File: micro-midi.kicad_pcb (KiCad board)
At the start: 2 copper layers, 40 x 27.5 mm, 14 parts, among them J1 AudioJack3, J2 Conn_01x04_Male, J3 AudioJack3, U1 74HC04, U2 6N137

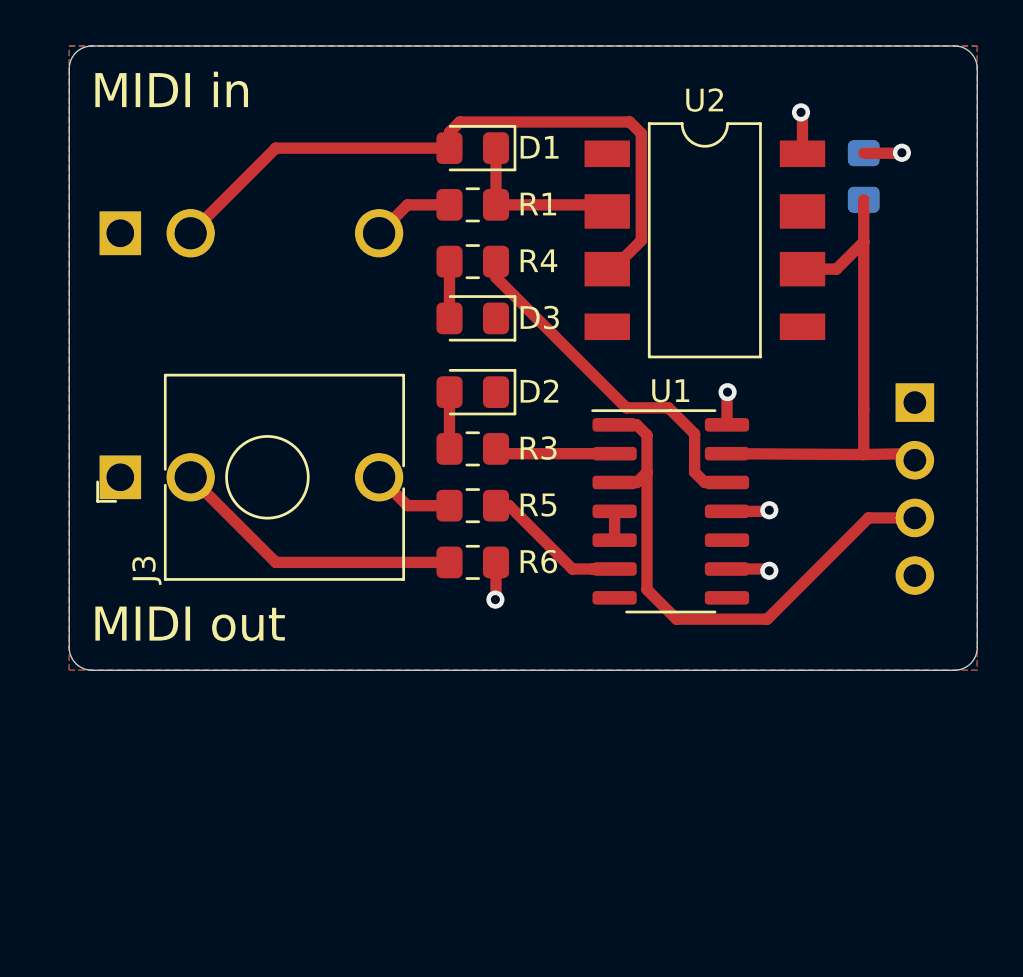
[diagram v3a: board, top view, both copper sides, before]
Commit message: fix accidentally flipped parts
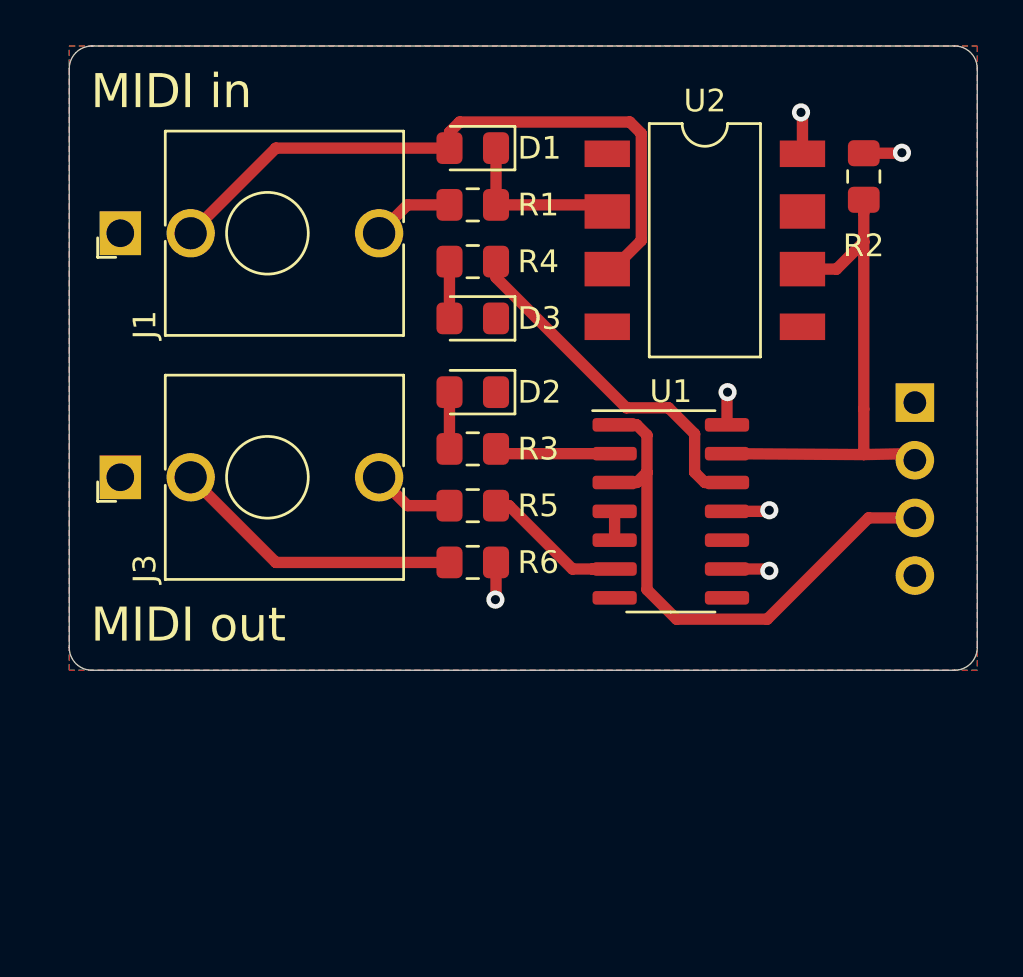
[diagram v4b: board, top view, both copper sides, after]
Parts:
- J1, R2: moved to F.Cu
- turned J1 to 90 degrees
- turned R2 to 90 degrees
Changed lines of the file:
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@@
   )
   (setup
-    (last_trace_width 0.5)
+    (last_trace_width 0.25)
     (user_trace_width 0.5)
     (trace_clearance 0.2)
@@
       (outputformat 1)
       (mirror false)
-      (drillshape 1)
+      (drillshape 0)
       (scaleselection 1)
-      (outputdirectory ""))
+      (outputdirectory "plot"))
   )
   (net 0 "")
@@
     )
   )
-  (module Connector_Audio:Jack_3.5mm_QingPu_WQP-PJ398SM_Vertical_CircularHoles (layer B.Cu)
-    (at 72.25 48.25 270)
+  (module Connector_Audio:Jack_3.5mm_QingPu_WQP-PJ398SM_Vertical_CircularHoles (layer F.Cu)
+    (at 72.25 48.25 90)
     (descr "TRS 3.5mm, vertical, Thonkiconn, PCB mount, (http://www.qingpu-electronics.com/en/products/WQP-PJ398SM-362.html)")
     (tags "WQP-PJ398SM WQP-PJ301M-12 TRS 3.5mm mono vertical jack thonkiconn qingpu")
-    (fp_text reference J1 (at -4.03 -1.08 90) (layer B.SilkS)
-      (effects (font (size 1 1) (thickness 0.15)) (justify mirror))
-    )
-    (fp_text value AudioJack3 (at 0 -5 90) (layer B.Fab)
-      (effects (font (size 1 1) (thickness 0.15)) (justify mirror))
-    )
-    (fp_line (start 0 0) (end 0 -2.03) (layer B.Fab) (width 0.1))
-    (fp_circle (center 0 -6.48) (end 1.8 -6.48) (layer B.Fab) (width 0.1))
-    (fp_line (start 4.5 -2.03) (end -4.5 -2.03) (layer B.Fab) (width 0.1))
-    (fp_line (start 5 1.42) (end -5 1.42) (layer B.CrtYd) (width 0.05))
-    (fp_line (start 5 -12.98) (end -5 -12.98) (layer B.CrtYd) (width 0.05))
-    (fp_line (start 5 -12.98) (end 5 1.42) (layer B.CrtYd) (width 0.05))
-    (fp_line (start 4.5 -12.48) (end -4.5 -12.48) (layer B.Fab) (width 0.1))
-    (fp_line (start 4.5 -12.48) (end 4.5 -2.08) (layer B.Fab) (width 0.1))
-    (fp_line (start -1.06 1) (end -0.2 1) (layer B.SilkS) (width 0.12))
-    (fp_line (start -1.06 1) (end -1.06 0.2) (layer B.SilkS) (width 0.12))
-    (fp_circle (center 0 -6.48) (end 1.8 -6.48) (layer B.SilkS) (width 0.12))
-    (fp_line (start -0.35 -1.98) (end -4.5 -1.98) (layer B.SilkS) (width 0.12))
-    (fp_line (start 4.5 -1.98) (end 0.35 -1.98) (layer B.SilkS) (width 0.12))
-    (fp_line (start -0.5 -12.48) (end -4.5 -12.48) (layer B.SilkS) (width 0.12))
-    (fp_line (start 4.5 -12.48) (end 0.5 -12.48) (layer B.SilkS) (width 0.12))
-    (fp_line (start -1.41 -6.02) (end -0.46 -5.07) (layer Dwgs.User) (width 0.12))
-    (fp_line (start -1.42 -6.875) (end 0.4 -5.06) (layer Dwgs.User) (width 0.12))
-    (fp_line (start -1.07 -7.49) (end 1.01 -5.41) (layer Dwgs.User) (width 0.12))
-    (fp_line (start -0.58 -7.83) (end 1.36 -5.89) (layer Dwgs.User) (width 0.12))
-    (fp_line (start 0.09 -7.96) (end 1.48 -6.57) (layer Dwgs.User) (width 0.12))
-    (fp_circle (center 0 -6.48) (end 1.5 -6.48) (layer Dwgs.User) (width 0.12))
-    (fp_line (start 4.5 -1.98) (end 4.5 -12.48) (layer B.SilkS) (width 0.12))
-    (fp_line (start -4.5 -1.98) (end -4.5 -12.48) (layer B.SilkS) (width 0.12))
-    (fp_text user %R (at 0 -8 90) (layer B.Fab)
-      (effects (font (size 1 1) (thickness 0.15)) (justify mirror))
-    )
-    (fp_line (start -4.5 -12.48) (end -4.5 -2.08) (layer B.Fab) (width 0.1))
-    (fp_line (start -5 -12.98) (end -5 1.42) (layer B.CrtYd) (width 0.05))
-    (fp_text user KEEPOUT (at 0 -6.48 270) (layer Cmts.User)
+    (fp_text reference J1 (at -4.03 1.08 270) (layer F.SilkS)
+      (effects (font (size 1 1) (thickness 0.15)))
+    )
+    (fp_text value AudioJack3 (at 0 5 270) (layer F.Fab)
+      (effects (font (size 1 1) (thickness 0.15)))
+    )
+    (fp_line (start 0 0) (end 0 2.03) (layer F.Fab) (width 0.1))
+    (fp_circle (center 0 6.48) (end 1.8 6.48) (layer F.Fab) (width 0.1))
+    (fp_line (start 4.5 2.03) (end -4.5 2.03) (layer F.Fab) (width 0.1))
+    (fp_line (start 5 -1.42) (end -5 -1.42) (layer F.CrtYd) (width 0.05))
+    (fp_line (start 5 12.98) (end -5 12.98) (layer F.CrtYd) (width 0.05))
+    (fp_line (start 5 12.98) (end 5 -1.42) (layer F.CrtYd) (width 0.05))
+    (fp_line (start 4.5 12.48) (end -4.5 12.48) (layer F.Fab) (width 0.1))
+    (fp_line (start 4.5 12.48) (end 4.5 2.08) (layer F.Fab) (width 0.1))
+    (fp_line (start -1.06 -1) (end -0.2 -1) (layer F.SilkS) (width 0.12))
+    (fp_line (start -1.06 -1) (end -1.06 -0.2) (layer F.SilkS) (width 0.12))
+    (fp_circle (center 0 6.48) (end 1.8 6.48) (layer F.SilkS) (width 0.12))
+    (fp_line (start -0.35 1.98) (end -4.5 1.98) (layer F.SilkS) (width 0.12))
+    (fp_line (start 4.5 1.98) (end 0.35 1.98) (layer F.SilkS) (width 0.12))
+    (fp_line (start -0.5 12.48) (end -4.5 12.48) (layer F.SilkS) (width 0.12))
+    (fp_line (start 4.5 12.48) (end 0.5 12.48) (layer F.SilkS) (width 0.12))
+    (fp_line (start -1.41 6.02) (end -0.46 5.07) (layer Dwgs.User) (width 0.12))
+    (fp_line (start -1.42 6.875) (end 0.4 5.06) (layer Dwgs.User) (width 0.12))
+    (fp_line (start -1.07 7.49) (end 1.01 5.41) (layer Dwgs.User) (width 0.12))
+    (fp_line (start -0.58 7.83) (end 1.36 5.89) (layer Dwgs.User) (width 0.12))
+    (fp_line (start 0.09 7.96) (end 1.48 6.57) (layer Dwgs.User) (width 0.12))
+    (fp_circle (center 0 6.48) (end 1.5 6.48) (layer Dwgs.User) (width 0.12))
+    (fp_line (start 4.5 1.98) (end 4.5 12.48) (layer F.SilkS) (width 0.12))
+    (fp_line (start -4.5 1.98) (end -4.5 12.48) (layer F.SilkS) (width 0.12))
+    (fp_text user %R (at 0 8 270) (layer F.Fab)
+      (effects (font (size 1 1) (thickness 0.15)))
+    )
+    (fp_line (start -4.5 12.48) (end -4.5 2.08) (layer F.Fab) (width 0.1))
+    (fp_line (start -5 12.98) (end -5 -1.42) (layer F.CrtYd) (width 0.05))
+    (fp_text user KEEPOUT (at 0 6.48 90) (layer Cmts.User)
       (effects (font (size 0.4 0.4) (thickness 0.051)))
     )
-    (pad T thru_hole circle (at 0 -11.4 90) (size 2.13 2.13) (drill 1.43) (layers *.Cu *.Mask)
+    (pad T thru_hole circle (at 0 11.4 270) (size 2.13 2.13) (drill 1.43) (layers *.Cu *.Mask)
       (net 6 "Net-(J1-PadT)"))
-    (pad S thru_hole rect (at 0 0 90) (size 1.93 1.83) (drill 1.22) (layers *.Cu *.Mask))
-    (pad R thru_hole circle (at 0 -3.1 90) (size 2.13 2.13) (drill 1.42) (layers *.Cu *.Mask)
+    (pad S thru_hole rect (at 0 0 270) (size 1.93 1.83) (drill 1.22) (layers *.Cu *.Mask))
+    (pad R thru_hole circle (at 0 3.1 270) (size 2.13 2.13) (drill 1.42) (layers *.Cu *.Mask)
       (net 1 "Net-(D1-Pad2)"))
     (model ${KISYS3DMOD}/Connector_Audio.3dshapes/Jack_3.5mm_QingPu_WQP-PJ398SM_Vertical.wrl
@@
     )
   )
-  (module Resistor_SMD:R_0805_2012Metric_Pad1.15x1.40mm_HandSolder (layer B.Cu)
-    (at 105 45.75 270)
+  (module Resistor_SMD:R_0805_2012Metric_Pad1.15x1.40mm_HandSolder (layer F.Cu)
+    (at 105 45.75 90)
     (descr "Resistor SMD 0805 (2012 Metric), square (rectangular) end terminal, IPC_7351 nominal with elongated pad for handsoldering. (Body size source: https://docs.google.com/spreadsheets/d/1BsfQQcO9C6DZCsRaXUlFlo91Tg2WpOkGARC1WS5S8t0/edit?usp=sharing), generated with kicad-footprint-generator")
     (tags "resistor handsolder")
     (attr smd)
-    (fp_text reference R2 (at -3.048 0.009 180) (layer B.SilkS)
-      (effects (font (size 1 1) (thickness 0.15)) (justify mirror))
-    )
-    (fp_text value 10K (at 0 -1.65 270) (layer B.Fab)
-      (effects (font (size 1 1) (thickness 0.15)) (justify mirror))
-    )
-    (fp_line (start -1 -0.6) (end -1 0.6) (layer B.Fab) (width 0.1))
-    (fp_line (start -1 0.6) (end 1 0.6) (layer B.Fab) (width 0.1))
-    (fp_line (start 1 0.6) (end 1 -0.6) (layer B.Fab) (width 0.1))
-    (fp_line (start 1 -0.6) (end -1 -0.6) (layer B.Fab) (width 0.1))
-    (fp_line (start -0.261252 0.71) (end 0.261252 0.71) (layer B.SilkS) (width 0.12))
-    (fp_line (start -0.261252 -0.71) (end 0.261252 -0.71) (layer B.SilkS) (width 0.12))
-    (fp_line (start -1.85 -0.95) (end -1.85 0.95) (layer B.CrtYd) (width 0.05))
-    (fp_line (start -1.85 0.95) (end 1.85 0.95) (layer B.CrtYd) (width 0.05))
-    (fp_line (start 1.85 0.95) (end 1.85 -0.95) (layer B.CrtYd) (width 0.05))
-    (fp_line (start 1.85 -0.95) (end -1.85 -0.95) (layer B.CrtYd) (width 0.05))
-    (fp_text user %R (at 0 0 270) (layer B.Fab)
-      (effects (font (size 0.5 0.5) (thickness 0.08)) (justify mirror))
-    )
-    (pad 1 smd roundrect (at -1.025 0 270) (size 1.15 1.4) (layers B.Cu B.Paste B.Mask) (roundrect_rratio 0.217391)
+    (fp_text reference R2 (at -3.048 -0.009 180) (layer F.SilkS)
+      (effects (font (size 1 1) (thickness 0.15)))
+    )
+    (fp_text value 10K (at 0 1.65 90) (layer F.Fab)
+      (effects (font (size 1 1) (thickness 0.15)))
+    )
+    (fp_line (start -1 0.6) (end -1 -0.6) (layer F.Fab) (width 0.1))
+    (fp_line (start -1 -0.6) (end 1 -0.6) (layer F.Fab) (width 0.1))
+    (fp_line (start 1 -0.6) (end 1 0.6) (layer F.Fab) (width 0.1))
+    (fp_line (start 1 0.6) (end -1 0.6) (layer F.Fab) (width 0.1))
+    (fp_line (start -0.261252 -0.71) (end 0.261252 -0.71) (layer F.SilkS) (width 0.12))
+    (fp_line (start -0.261252 0.71) (end 0.261252 0.71) (layer F.SilkS) (width 0.12))
+    (fp_line (start -1.85 0.95) (end -1.85 -0.95) (layer F.CrtYd) (width 0.05))
+    (fp_line (start -1.85 -0.95) (end 1.85 -0.95) (layer F.CrtYd) (width 0.05))
+    (fp_line (start 1.85 -0.95) (end 1.85 0.95) (layer F.CrtYd) (width 0.05))
+    (fp_line (start 1.85 0.95) (end -1.85 0.95) (layer F.CrtYd) (width 0.05))
+    (fp_text user %R (at 0 0 90) (layer F.Fab)
+      (effects (font (size 0.5 0.5) (thickness 0.08)))
+    )
+    (pad 1 smd roundrect (at -1.025 0 90) (size 1.15 1.4) (layers F.Cu F.Paste F.Mask) (roundrect_rratio 0.217391)
       (net 4 "Net-(J2-Pad2)"))
-    (pad 2 smd roundrect (at 1.025 0 270) (size 1.15 1.4) (layers B.Cu B.Paste B.Mask) (roundrect_rratio 0.217391)
+    (pad 2 smd roundrect (at 1.025 0 90) (size 1.15 1.4) (layers F.Cu F.Paste F.Mask) (roundrect_rratio 0.217391)
       (net 3 +5V))
     (model ${KISYS3DMOD}/Resistor_SMD.3dshapes/R_0805_2012Metric.wrl

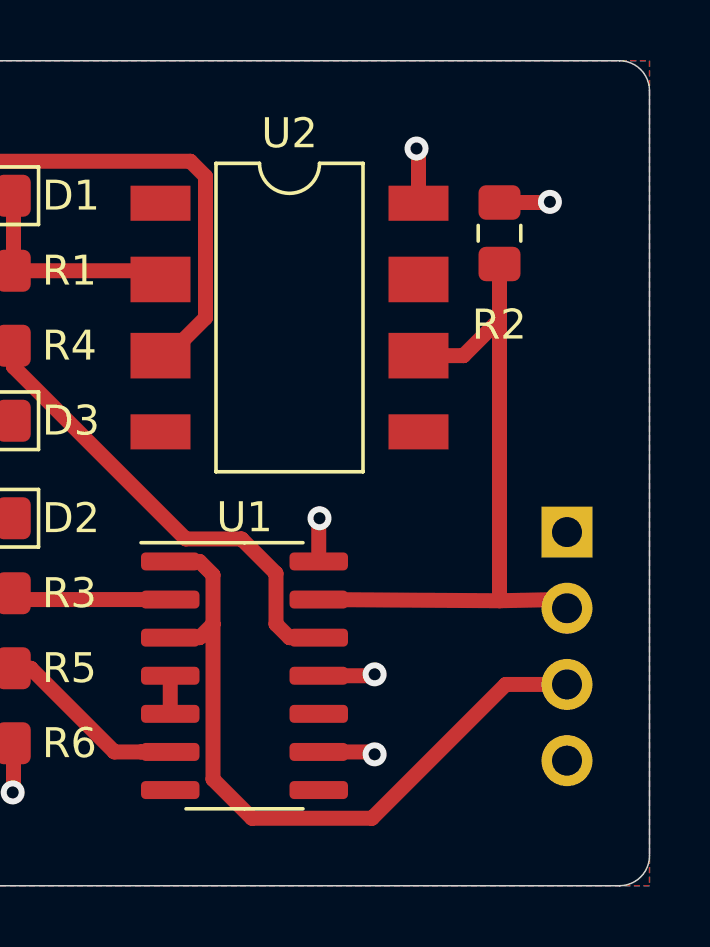
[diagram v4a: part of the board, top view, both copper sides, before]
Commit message: move r2 to make some room
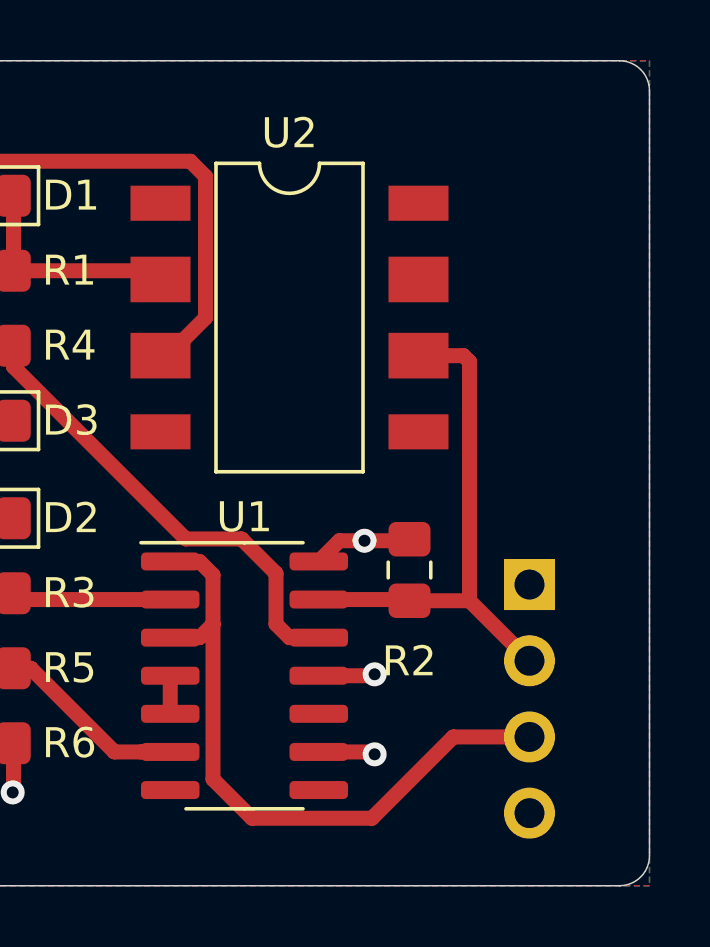
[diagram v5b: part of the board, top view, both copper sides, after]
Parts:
- moved R2 11.6 mm to (102.0, 57.0)
- moved J2 2.15 mm to (106.0, 57.5)
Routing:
- net Net-(J2-Pad2): track 22.8 -> 17.6 mm
- net Net-(J2-Pad3): track 24.2 -> 22.2 mm
- net +5V: track 10.4 -> 8.76 mm, vias 6 -> 4
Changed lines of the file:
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@@
     (thickness 1.6)
     (drawings 10)
-    (tracks 71)
+    (tracks 65)
     (zones 0)
     (modules 14)
@@
   (layers
     (0 F.Cu signal)
-    (31 B.Cu signal)
+    (31 B.Cu signal hide)
     (32 B.Adhes user)
     (33 F.Adhes user)
@@
   )
   (setup
-    (last_trace_width 0.25)
+    (last_trace_width 0.5)
     (user_trace_width 0.5)
     (trace_clearance 0.2)
@@
   )
   (module Connector_PinHeader_2.54mm:PinHeader_1x04_P2.54mm_Vertical (layer B.Cu)
-    (at 107.25 55.71 180)
+    (at 106 57.46 180)
     (descr "Through hole straight pin header, 1x04, 2.54mm pitch, single row")
     (tags "Through hole pin header THT 1x04 2.54mm single row")
@@
   )
   (module Resistor_SMD:R_0805_2012Metric_Pad1.15x1.40mm_HandSolder (layer F.Cu)
-    (at 105 45.75 90)
+    (at 102 56.975 90)
     (descr "Resistor SMD 0805 (2012 Metric), square (rectangular) end terminal, IPC_7351 nominal with elongated pad for handsoldering. (Body size source: https://docs.google.com/spreadsheets/d/1BsfQQcO9C6DZCsRaXUlFlo91Tg2WpOkGARC1WS5S8t0/edit?usp=sharing), generated with kicad-footprint-generator")
     (tags "resistor handsolder")
@@
   (segment (start 88.8 47) (end 93.41 47) (width 0.5) (layer F.Cu) (net 2))
   (segment (start 88.8 47) (end 88.8 44.5) (width 0.5) (layer F.Cu) (net 2))
-  (segment (start 98.975 56.69) (end 98.975 55.275) (width 0.5) (layer F.Cu) (net 3))
-  (via (at 99 55.25) (size 0.8) (drill 0.4) (layers F.Cu B.Cu) (net 3))
-  (segment (start 98.975 55.275) (end 99 55.25) (width 0.5) (layer F.Cu) (net 3))
   (via (at 100.838 63.119) (size 0.8) (drill 0.4) (layers F.Cu B.Cu) (net 3))
   (segment (start 98.975 63.04) (end 100.759 63.04) (width 0.5) (layer F.Cu) (net 3))
@@
   (segment (start 88.8 62.75) (end 88.8 64.362) (width 0.5) (layer F.Cu) (net 3))
   (segment (start 88.8 64.362) (end 88.773 64.389) (width 0.5) (layer F.Cu) (net 3))
-  (via (at 106.68 44.704) (size 0.8) (drill 0.4) (layers F.Cu B.Cu) (net 3))
-  (segment (start 105 44.725) (end 106.659 44.725) (width 0.5) (layer F.Cu) (net 3))
-  (segment (start 106.659 44.725) (end 106.68 44.704) (width 0.5) (layer F.Cu) (net 3))
-  (via (at 102.235 42.926) (size 0.8) (drill 0.4) (layers F.Cu B.Cu) (net 3))
-  (segment (start 102.3 44.75) (end 102.3 42.991) (width 0.5) (layer F.Cu) (net 3))
-  (segment (start 102.3 42.991) (end 102.235 42.926) (width 0.5) (layer F.Cu) (net 3))
-  (segment (start 106.96 57.96) (end 107.25 58.25) (width 0.5) (layer F.Cu) (net 4))
-  (segment (start 105 47.35) (end 105 46.775) (width 0.5) (layer F.Cu) (net 4))
-  (segment (start 105 48.63) (end 105 47.35) (width 0.5) (layer F.Cu) (net 4))
-  (segment (start 103.8 49.83) (end 105 48.63) (width 0.5) (layer F.Cu) (net 4))
-  (segment (start 102.3 49.83) (end 103.8 49.83) (width 0.5) (layer F.Cu) (net 4))
-  (segment (start 105 48.63) (end 105 56) (width 0.5) (layer F.Cu) (net 4))
-  (segment (start 98.975 57.96) (end 105 58) (width 0.5) (layer F.Cu) (net 4))
-  (segment (start 105 56) (end 105 58) (width 0.5) (layer F.Cu) (net 4))
-  (segment (start 105 58) (end 106.96 57.96) (width 0.5) (layer F.Cu) (net 4))
+  (segment (start 101.96 57.96) (end 102 58) (width 0.5) (layer F.Cu) (net 4))
+  (segment (start 98.975 57.96) (end 101.96 57.96) (width 0.5) (layer F.Cu) (net 4))
+  (segment (start 104 58) (end 106 60) (width 0.5) (layer F.Cu) (net 4))
+  (segment (start 102 58) (end 104 58) (width 0.5) (layer F.Cu) (net 4))
+  (segment (start 103.8 49.83) (end 102.3 49.83) (width 0.5) (layer F.Cu) (net 4))
+  (segment (start 104 50.03) (end 103.8 49.83) (width 0.5) (layer F.Cu) (net 4))
+  (segment (start 104 58) (end 104 50.03) (width 0.5) (layer F.Cu) (net 4))
+  (via (at 100.5 56) (size 0.8) (drill 0.4) (layers F.Cu B.Cu) (net 3))
+  (segment (start 101.95 56) (end 102 55.95) (width 0.5) (layer F.Cu) (net 3))
+  (segment (start 100.5 56) (end 101.95 56) (width 0.5) (layer F.Cu) (net 3))
+  (segment (start 99.665 56) (end 98.975 56.69) (width 0.5) (layer F.Cu) (net 3))
+  (segment (start 100.5 56) (end 99.665 56) (width 0.5) (layer F.Cu) (net 3))
   (segment (start 83.65 48.25) (end 84.9 47) (width 0.5) (layer F.Cu) (net 6))
   (segment (start 84.9 47) (end 86.75 47) (width 0.5) (layer F.Cu) (net 6))
@@
   (segment (start 95 59.23) (end 95.45001 58.77999) (width 0.5) (layer F.Cu) (net 9))
   (segment (start 94.025 59.23) (end 95 59.23) (width 0.5) (layer F.Cu) (net 9))
-  (segment (start 105.21 60.79) (end 107.25 60.79) (width 0.5) (layer F.Cu) (net 9))
-  (segment (start 100.75 65.25) (end 105.21 60.79) (width 0.5) (layer F.Cu) (net 9))
   (segment (start 96.75 65.25) (end 100.75 65.25) (width 0.5) (layer F.Cu) (net 9))
   (segment (start 95.45001 58.77999) (end 95.45001 63.95001) (width 0.5) (layer F.Cu) (net 9))
   (segment (start 95.45001 63.95001) (end 96.75 65.25) (width 0.5) (layer F.Cu) (net 9))
+  (segment (start 103.46 62.54) (end 100.75 65.25) (width 0.5) (layer F.Cu) (net 9))
+  (segment (start 106 62.54) (end 103.46 62.54) (width 0.5) (layer F.Cu) (net 9))
   (segment (start 83.65 59) (end 84.9 60.25) (width 0.5) (layer F.Cu) (net 10))
   (segment (start 84.9 60.25) (end 86.75 60.25) (width 0.5) (layer F.Cu) (net 10))
